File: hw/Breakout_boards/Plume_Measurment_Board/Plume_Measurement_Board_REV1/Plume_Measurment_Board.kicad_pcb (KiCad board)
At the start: 2 copper layers, 42 parts, among them J2 Conn_01x04, J4 Conn_01x04, U2 LMP7721MA/NOPB, U3 LMP2022MA/NOPB, U4 AD8475ARMZ, U5 AD8475ARMZ, U6 TPS62153, U7 AD7176-2BRUZ

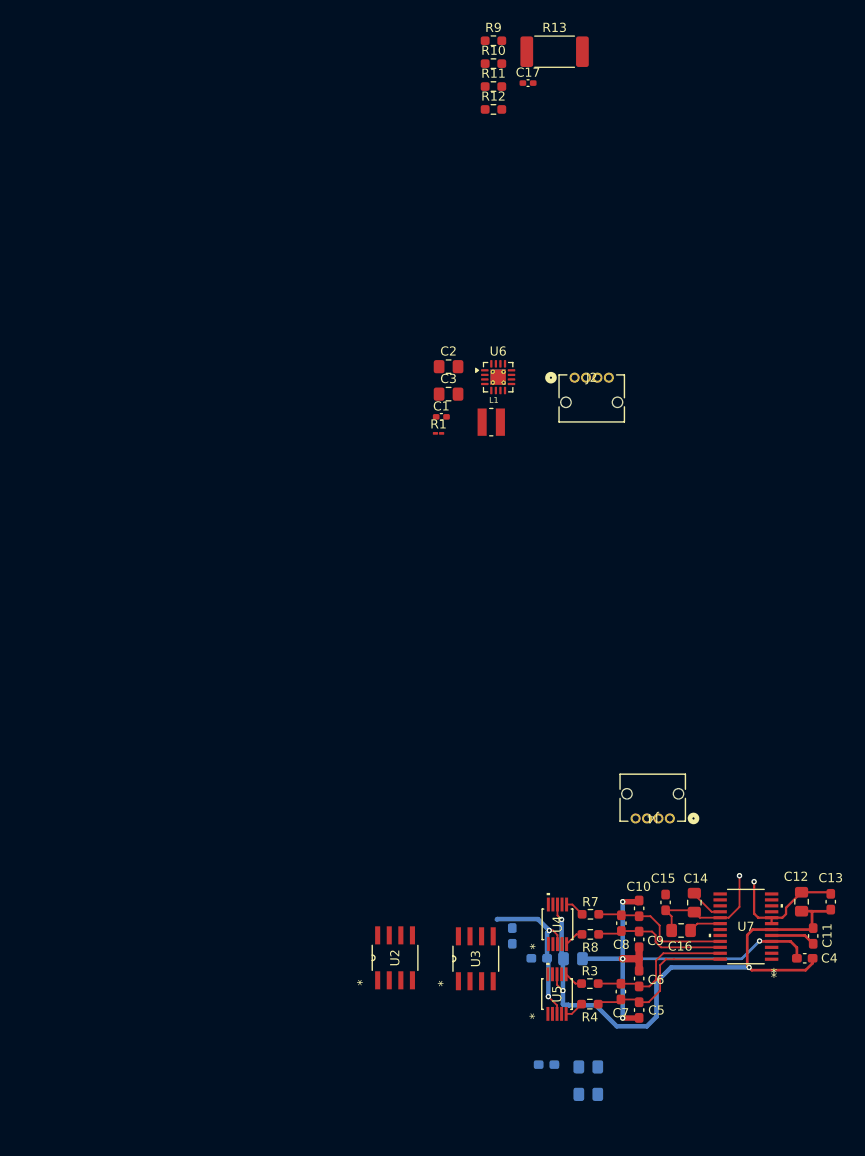
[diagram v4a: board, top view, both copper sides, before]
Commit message: MAX31856 Driver Full Integrations
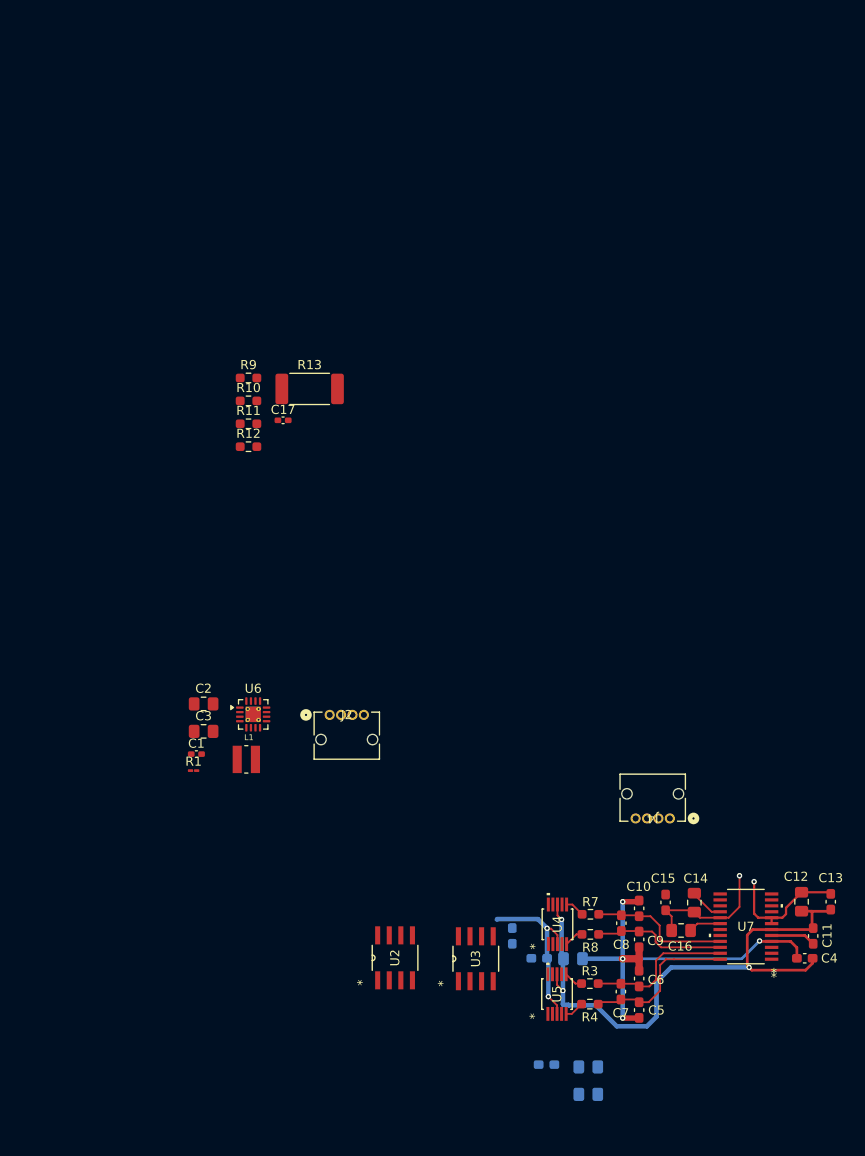
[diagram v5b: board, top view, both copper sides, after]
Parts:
- moved R1 45.7 mm to (67.1, 31.2)
- moved R10 45.7 mm to (73.1, -9.29)
- moved C1 45.7 mm to (67.4, 29.4)
- moved C17 45.7 mm to (76.9, -7.16)
- moved C2 45.7 mm to (68.2, 23.9)
- moved C3 45.7 mm to (68.2, 26.9)
- moved J2 45.7 mm to (82.0, 25.1)
- moved L1 45.7 mm to (72.9, 30.0)
- moved R11 45.7 mm to (73.1, -6.78)
- moved R12 45.7 mm to (73.1, -4.27)
- moved R13 45.7 mm to (79.8, -10.6)
- moved R9 45.7 mm to (73.1, -11.8)
- moved U6 45.7 mm to (73.7, 25.1)
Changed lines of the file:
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@@
 	(footprint "Resistor_SMD:R_2512_6332Metric_Pad1.40x3.35mm_HandSolder"
 		(layer "F.Cu")
-		(at 106.685 -47.5575)
+		(at 79.84 -10.598599)
 		(descr "Resistor SMD 2512 (6332 Metric), square (rectangular) end terminal, IPC-7351 nominal with elongated pad for handsoldering. (Body size source: IPC-SM-782 page 72, https://www.pcb-3d.com/wordpress/wp-content/uploads/ipc-sm-782a_amendment_1_and_2.pdf)")
 		(tags "resistor handsolder")
@@
 	(footprint "Resistor_SMD:R_0603_1608Metric_Pad0.98x0.95mm_HandSolder"
 		(layer "F.Cu")
-		(at 99.985 -48.7575)
+		(at 73.14 -11.798599)
 		(descr "Resistor SMD 0603 (1608 Metric), square (rectangular) end terminal, IPC-7351 nominal with elongated pad for handsoldering. (Body size source: IPC-SM-782 page 72, https://www.pcb-3d.com/wordpress/wp-content/uploads/ipc-sm-782a_amendment_1_and_2.pdf)")
 		(tags "resistor handsolder")
@@
 	(footprint "Resistor_SMD:R_01005_0402Metric_Pad0.57x0.30mm_HandSolder"
 		(layer "F.Cu")
-		(at 93.965 -5.7275)
+		(at 67.12 31.231401)
 		(descr "Resistor SMD 01005 (0402 Metric), square (rectangular) end terminal, IPC-7351 nominal with elongated pad for handsoldering. (Body size source: http://www.vishay.com/docs/20056/crcw01005e3.pdf)")
 		(tags "resistor handsolder")
@@
 	(footprint "Connector_Molex_Micro-Lock-Plus:Molex_Micro-Lock_2200980471_1x04_P1.25mm_Horizontal"
 		(layer "F.Cu")
-		(at 108.8804 -11.8327)
+		(at 82.0354 25.126201)
 		(tags "2200980471 ")
 		(property "Reference" "J2"
@@
 	(footprint "Capacitor_SMD:C_0402_1005Metric_Pad0.74x0.62mm_HandSolder"
 		(layer "F.Cu")
-		(at 103.775 -44.1175)
+		(at 76.93 -7.158599)
 		(descr "Capacitor SMD 0402 (1005 Metric), square (rectangular) end terminal, IPC-7351 nominal with elongated pad for handsoldering. (Body size source: IPC-SM-782 page 76, https://www.pcb-3d.com/wordpress/wp-content/uploads/ipc-sm-782a_amendment_1_and_2.pdf)")
 		(tags "capacitor handsolder")
@@
 	(footprint "Capacitor_SMD:C_0805_2012Metric_Pad1.18x1.45mm_HandSolder"
 		(layer "F.Cu")
-		(at 95.065 -13.0375)
+		(at 68.22 23.921401)
 		(descr "Capacitor SMD 0805 (2012 Metric), square (rectangular) end terminal, IPC-7351 nominal with elongated pad for handsoldering. (Body size source: IPC-SM-782 page 76, https://www.pcb-3d.com/wordpress/wp-content/uploads/ipc-sm-782a_amendment_1_and_2.pdf, https://docs.google.com/spreadsheets/d/1BsfQQcO9C6DZCsRaXUlFlo91Tg2WpOkGARC1WS5S8t0/edit?usp=sharing)")
 		(tags "capacitor handsolder")
@@
 	(footprint "Resistor_SMD:R_0603_1608Metric_Pad0.98x0.95mm_HandSolder"
 		(layer "F.Cu")
-		(at 99.985 -43.7375)
+		(at 73.14 -6.778599)
 		(descr "Resistor SMD 0603 (1608 Metric), square (rectangular) end terminal, IPC-7351 nominal with elongated pad for handsoldering. (Body size source: IPC-SM-782 page 72, https://www.pcb-3d.com/wordpress/wp-content/uploads/ipc-sm-782a_amendment_1_and_2.pdf)")
 		(tags "resistor handsolder")
@@
 	(footprint "Resistor_SMD:R_0603_1608Metric_Pad0.98x0.95mm_HandSolder"
 		(layer "F.Cu")
-		(at 99.985 -41.2275)
+		(at 73.14 -4.268599)
 		(descr "Resistor SMD 0603 (1608 Metric), square (rectangular) end terminal, IPC-7351 nominal with elongated pad for handsoldering. (Body size source: IPC-SM-782 page 72, https://www.pcb-3d.com/wordpress/wp-content/uploads/ipc-sm-782a_amendment_1_and_2.pdf)")
 		(tags "resistor handsolder")
@@
 	(footprint "Capacitor_SMD:C_0805_2012Metric_Pad1.18x1.45mm_HandSolder"
 		(layer "F.Cu")
-		(at 95.065 -10.0275)
+		(at 68.22 26.931401)
 		(descr "Capacitor SMD 0805 (2012 Metric), square (rectangular) end terminal, IPC-7351 nominal with elongated pad for handsoldering. (Body size source: IPC-SM-782 page 76, https://www.pcb-3d.com/wordpress/wp-content/uploads/ipc-sm-782a_amendment_1_and_2.pdf, https://docs.google.com/spreadsheets/d/1BsfQQcO9C6DZCsRaXUlFlo91Tg2WpOkGARC1WS5S8t0/edit?usp=sharing)")
 		(tags "capacitor handsolder")
@@
 	(footprint "Package_DFN_QFN:VQFN-16-1EP_3x3mm_P0.5mm_EP1.68x1.68mm_ThermalVias"
 		(layer "F.Cu")
-		(at 100.5 -11.8875)
+		(at 73.655 25.071401)
 		(descr "VQFN, 16 Pin (http://www.ti.com/lit/ds/symlink/tlv62095.pdf)")
 		(tags "VQFN NoLead")
@@
 	(footprint "Resistor_SMD:R_0603_1608Metric_Pad0.98x0.95mm_HandSolder"
 		(layer "F.Cu")
-		(at 99.985 -46.2475)
+		(at 73.14 -9.288599)
 		(descr "Resistor SMD 0603 (1608 Metric), square (rectangular) end terminal, IPC-7351 nominal with elongated pad for handsoldering. (Body size source: IPC-SM-782 page 72, https://www.pcb-3d.com/wordpress/wp-content/uploads/ipc-sm-782a_amendment_1_and_2.pdf)")
 		(tags "resistor handsolder")
@@
 	(footprint "Capacitor_SMD:C_0402_1005Metric_Pad0.74x0.62mm_HandSolder"
 		(layer "F.Cu")
-		(at 94.275 -7.5375)
+		(at 67.43 29.421401)
 		(descr "Capacitor SMD 0402 (1005 Metric), square (rectangular) end terminal, IPC-7351 nominal with elongated pad for handsoldering. (Body size source: IPC-SM-782 page 76, https://www.pcb-3d.com/wordpress/wp-content/uploads/ipc-sm-782a_amendment_1_and_2.pdf)")
 		(tags "capacitor handsolder")
@@
 	(footprint "Inductor_TDK:IND_VLS3012CX-2R2M-1"
 		(layer "F.Cu")
-		(at 99.745 -6.9575)
+		(at 72.9 30.001401)
 		(property "Reference" "L1"
 			(at 0.282 -2.4064 0)
@@
 	)
 	(segment
-		(start 106.5 48.75)
-		(end 107.000001 49.250001)
-		(width 0.2)
+		(start 132.05 46.2625)
+		(end 132.05 46.95)
+		(width 0.25)
 		(layer "F.Cu")
 		(net "+5V")
 	)
 	(segment
-		(start 132.05 46.2625)
-		(end 132.05 46.95)
-		(width 0.25)
+		(start 106.3 48.55)
+		(end 107.000001 49.250001)
+		(width 0.2)
 		(layer "F.Cu")
 		(net "+5V")
@@
 	)
 	(segment
-		(start 107.000001 49.250001)
-		(end 107.000001 50.25)
+		(start 105.8625 48.5125)
+		(end 105.9 48.55)
 		(width 0.2)
 		(layer "F.Cu")
@@
 	)
 	(segment
-		(start 106.1 48.75)
-		(end 106.5 48.75)
+		(start 105.9 48.55)
+		(end 106.3 48.55)
 		(width 0.2)
 		(layer "F.Cu")
@@
 		(net "+5V")
 	)
+	(segment
+		(start 107.000001 49.250001)
+		(end 107.000001 50.25)
+		(width 0.2)
+		(layer "F.Cu")
+		(net "+5V")
+	)
 	(via
 		(at 106 56)
@@
 	)
 	(via
-		(at 106.1 48.75)
+		(at 105.8625 48.5125)
 		(size 0.6)
 		(drill 0.3)
@@
 	)
 	(segment
-		(start 105.8625 51.8)
-		(end 106 51.9375)
-		(width 0.5)
-		(layer "B.Cu")
-		(net "+5V")
-	)
-	(segment
-		(start 106.1 48.75)
-		(end 104.85 47.5)
+		(start 100.4 47.5)
+		(end 100.35 47.55)
 		(width 0.5)
 		(layer "B.Cu")
@@
 	)
 	(segment
-		(start 100.4 47.5)
-		(end 100.35 47.55)
+		(start 105.8625 51.8)
+		(end 106 51.9375)
 		(width 0.5)
 		(layer "B.Cu")
@@
 	)
 	(segment
-		(start 105.8625 48.9875)
-		(end 105.8625 51.8)
+		(start 106 51.9375)
+		(end 106 56)
 		(width 0.5)
 		(layer "B.Cu")
@@
 	)
 	(segment
-		(start 106.1 48.75)
-		(end 105.8625 48.9875)
+		(start 105.8625 48.5125)
+		(end 104.85 47.5)
 		(width 0.5)
 		(layer "B.Cu")
@@
 	)
 	(segment
-		(start 106 51.9375)
-		(end 106 56)
+		(start 105.8625 48.5125)
+		(end 105.8625 51.8)
 		(width 0.5)
 		(layer "B.Cu")

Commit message: 2nd Stage Amp Routing Progress
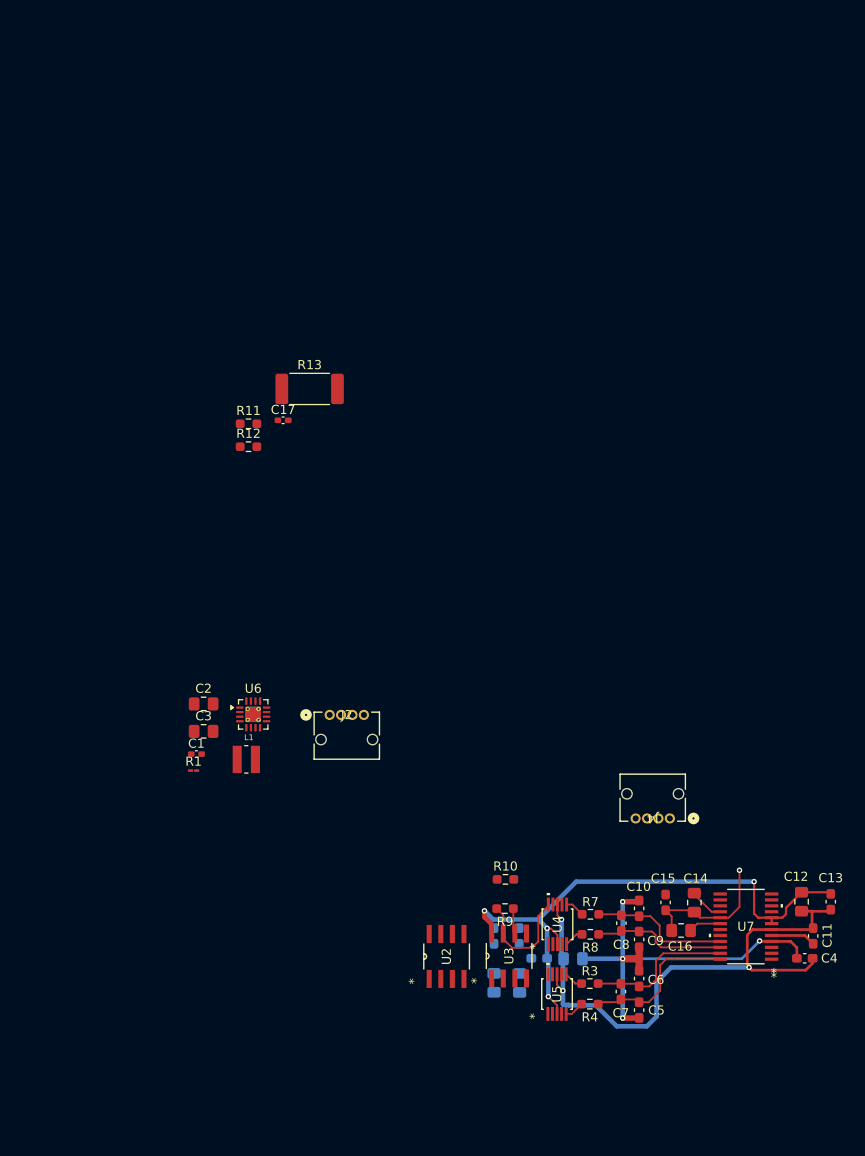
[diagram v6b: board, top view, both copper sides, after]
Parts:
- R10, R9: value ? -> 1000
- moved R9 64.6 mm to (101.2, 46.4), turned to 180 degrees
- moved R10 59.5 mm to (101.3, 43.1)
- moved C23 16.0 mm to (100.0, 54.5), turned to 90 degrees
- moved C20 15.2 mm to (100.0, 49.4), turned to 90 degrees
- moved C21 11.9 mm to (102.8, 54.5), turned to 90 degrees
- moved U2 5.65 mm to (94.8, 51.6)
- moved U3 3.66 mm to (101.7, 51.5)
- moved C22 0.75 mm to (102.8, 49.4)
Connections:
- R11 pad 2: /1_IN0.8+ -> /2_IN0.8+
- R9 pad 2: /2_IN0.8+ -> /1_IN0.8+
- U3 pad 1: /1_IN0.8+ -> /2_IN0.8+
- U3 pad 7: /2_IN0.8+ -> /1_IN0.8+
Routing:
- net +5V: track 32.6 -> 62.5 mm, vias 3 -> 4
- net /1_IN0.8+: track 0.00 -> 13.2 mm
- net Net-(U3A-INB-): track 0.00 -> 3.01 mm
- net GND: track 79.1 -> 79.7 mm

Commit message: First + Second Stage Amp Work
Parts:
- moved R11 68.7 mm to (100.4, 56.3), turned to 180 degrees
- moved R12 64.2 mm to (97.8, 55.0), turned to -90 degrees
- moved C3 39.7 mm to (105.9, 39.4), turned to 180 degrees
- moved U6 33.9 mm to (105.9, 35.4)
- moved C21 7.00 mm to (95.8, 54.5)
- moved C22 6.90 mm to (95.9, 49.5)
- moved R10 6.88 mm to (97.8, 49.1), turned to 90 degrees
- moved U2 0.85 mm to (94.0, 51.6)
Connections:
- U2 pad 1: GND -> /+2.5V
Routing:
- net /+2.5V: track 46.6 -> 148.5 mm, vias 4 -> 6
- net GND: track 79.7 -> 113.7 mm, vias 4 -> 6
- net /2_IN0.8+: track 0.00 -> 10.0 mm
- net Net-(U3A-INA-): track 0.00 -> 9.03 mm
- net Net-(U3A-INB-): track 3.01 -> 11.1 mm
- net +5V: track 62.5 -> 70.5 mm, vias 4 -> 5
- net /Amplified_Plume_1: track 0.00 -> 6.03 mm

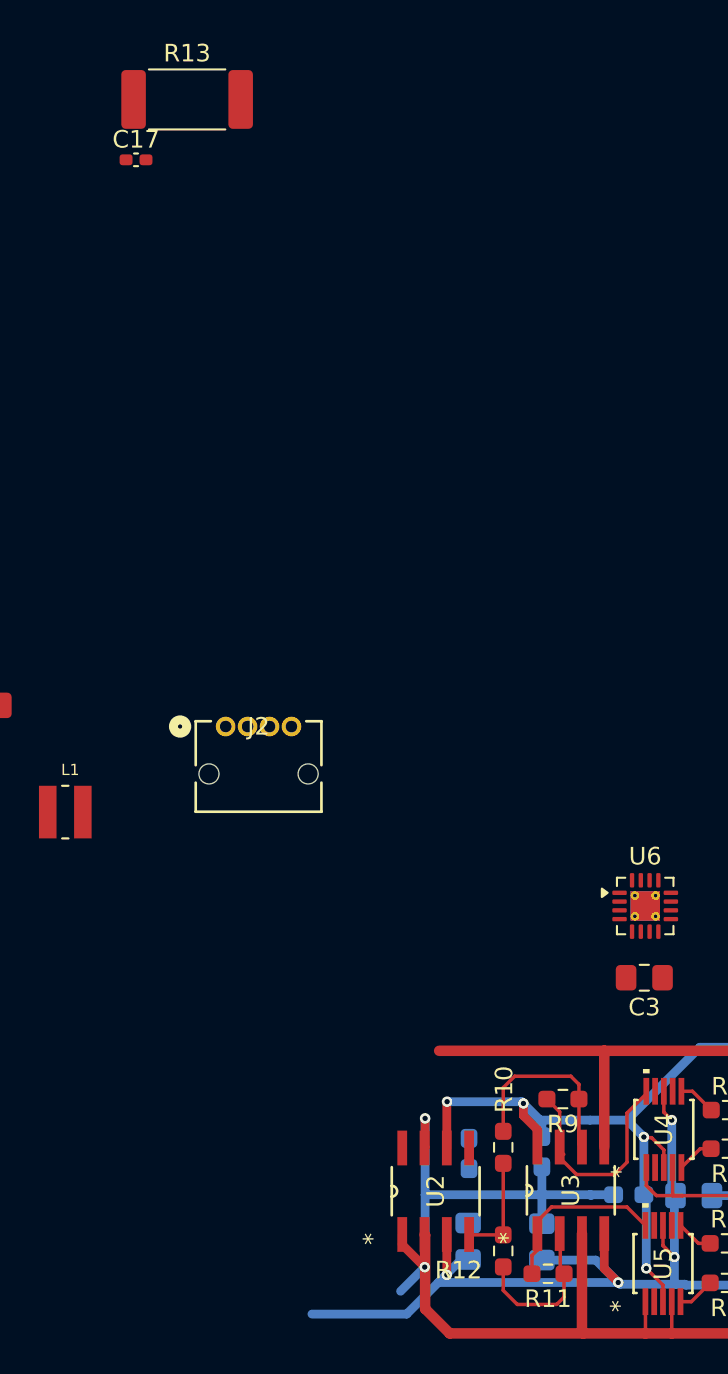
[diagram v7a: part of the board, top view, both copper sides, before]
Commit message: Entire RF pipeline
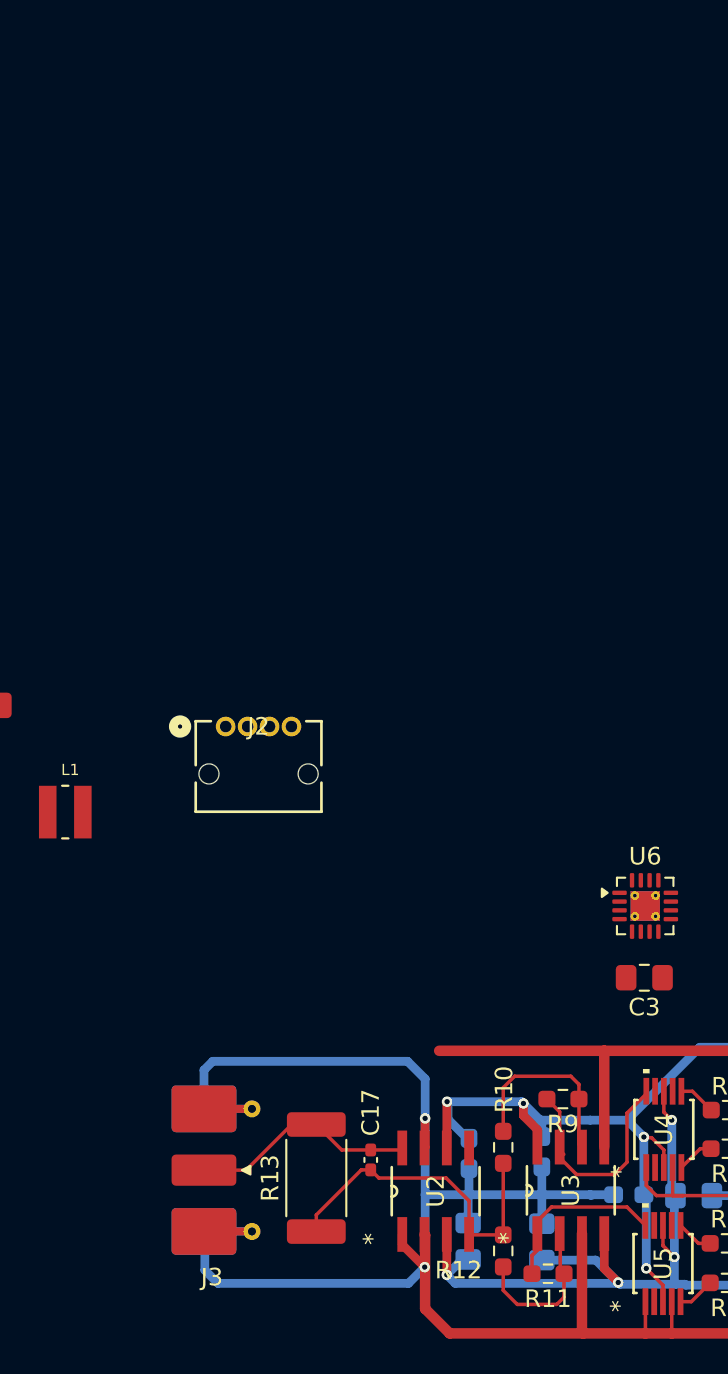
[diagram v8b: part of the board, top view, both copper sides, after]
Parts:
- added J3: Conn_Coaxial, Connector_Coaxial:SMA_Molex_73251-2120_EdgeMount_Horizontal, F.Cu at (80.5, 50.4)
- moved R13 61.9 mm to (87.2, 50.9), turned to 90 degrees
- moved C17 58.5 mm to (90.3, 49.8), turned to -90 degrees
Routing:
- net /+2.5V: track 148.5 -> 181.5 mm
- net /Amplified_Plume_1: track 6.03 -> 19.4 mm
- net /Plume: track 0.00 -> 13.2 mm
- net GND: track 113.7 -> 104.9 mm
- net +5V: track 70.5 -> 73.2 mm
